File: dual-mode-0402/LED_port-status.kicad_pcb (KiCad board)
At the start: 2 copper layers, 23.7 x 12.5 mm, 21 parts, among them P1 CONN_9

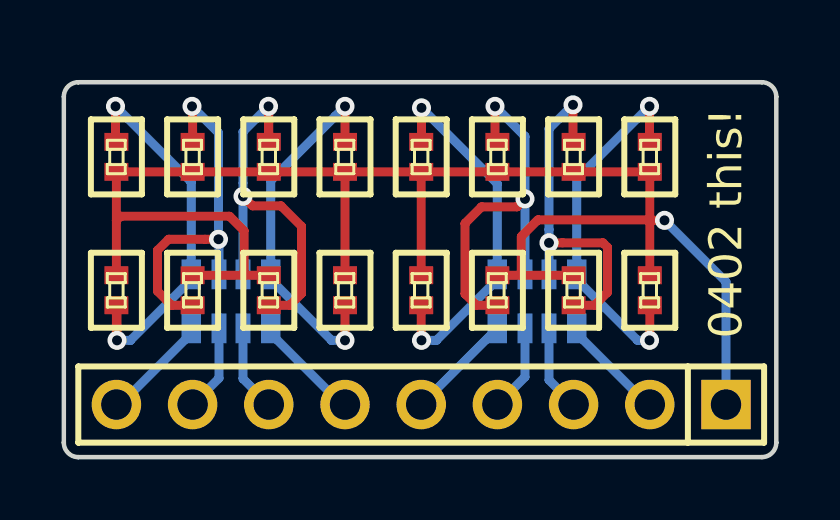
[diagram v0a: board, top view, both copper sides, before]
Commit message: Tweaked 'dual-mode-0402'.
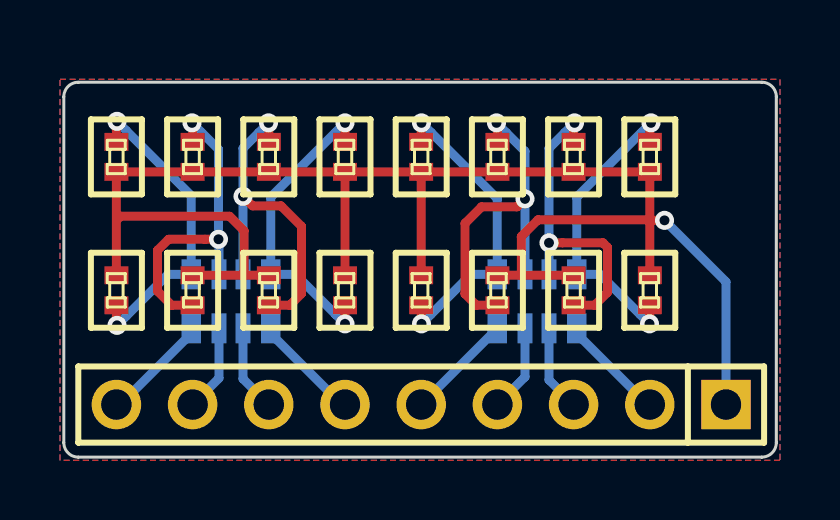
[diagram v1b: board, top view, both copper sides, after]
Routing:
- net Net-(D1-Pad2): track 13.7 -> 10.7 mm
- net Net-(D11-Pad1): track 14.2 -> 11.9 mm
- net Net-(D12-Pad1): track 12.5 -> 10.5 mm
- net Net-(D16-Pad1): track 12.4 -> 10.5 mm
- net Net-(D13-Pad1): track 12.4 -> 10.6 mm
- net Net-(D15-Pad1): track 12.0 -> 10.9 mm
- net Net-(D14-Pad1): track 13.2 -> 12.0 mm
- net Net-(D10-Pad1): track 12.1 -> 11.0 mm
- added copper zone on B.Cu, net Net-(D1-Pad1)
- added copper zone on F.Cu, net Net-(D1-Pad1)
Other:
- board text added: "blog.spitzenpfeil.org 2015 - V0.20.a"
- board text removed: "blog.spitzenpfeil.org 2015 - V0.20"
